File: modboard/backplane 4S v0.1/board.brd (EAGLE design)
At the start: 50 x 42 mm, 20 parts

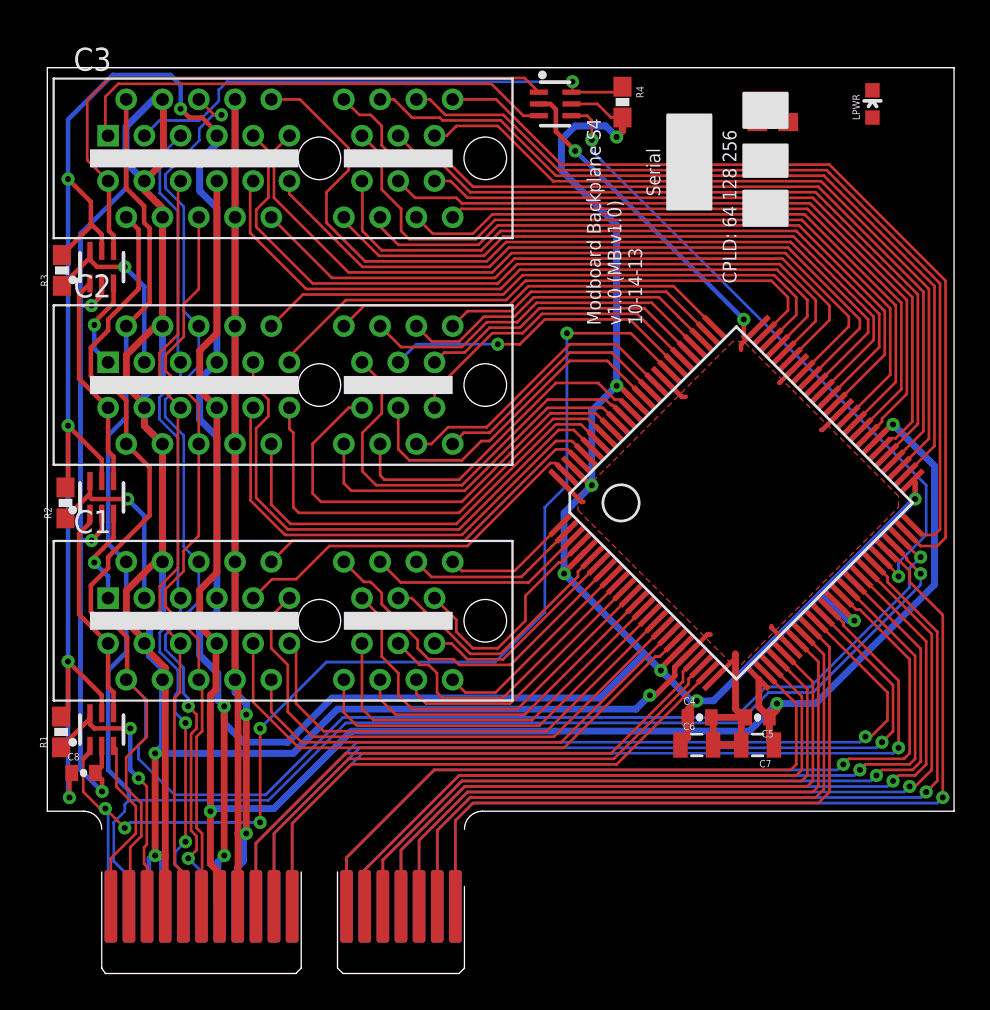
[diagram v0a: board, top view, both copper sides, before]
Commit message: rerouted parts of the modboard backplane to put the {2,3}{D,E} lanes on the NC lines
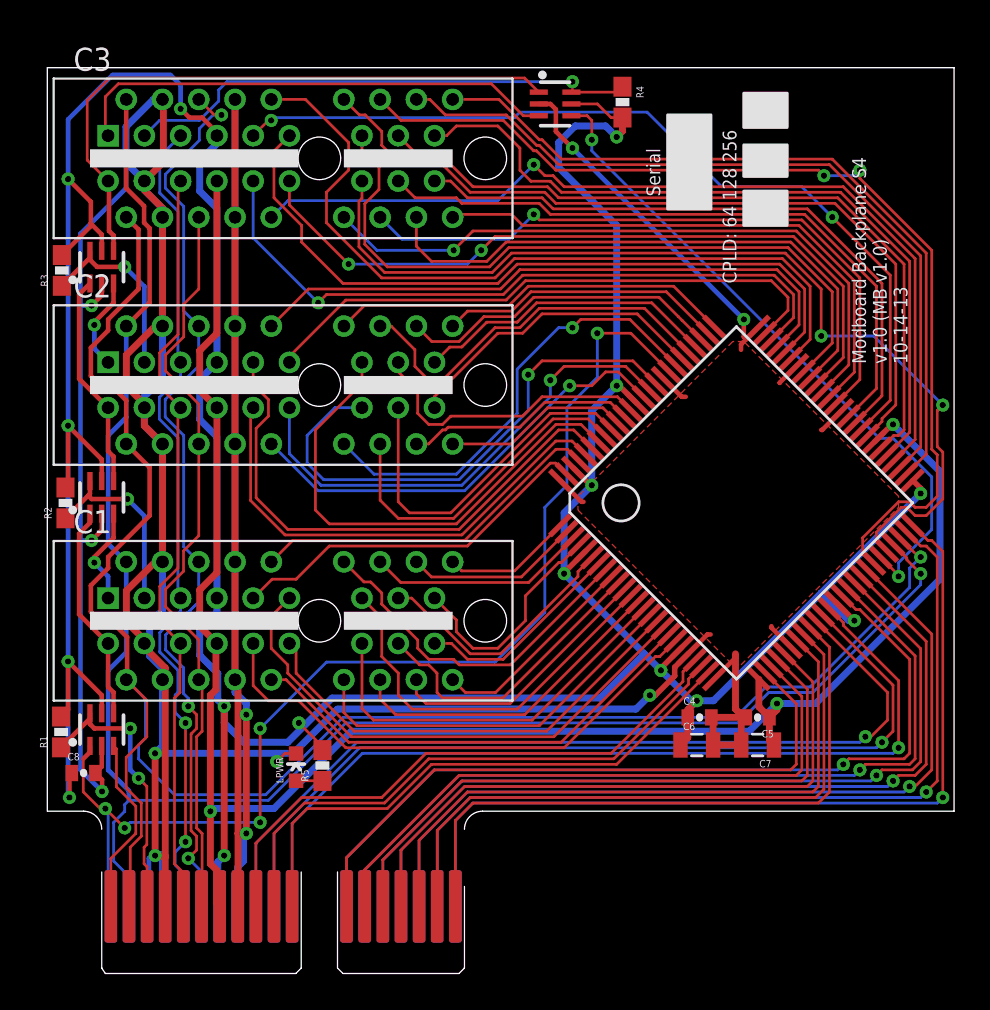
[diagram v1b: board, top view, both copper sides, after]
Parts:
- moved LPWR 48.5 mm to (13.7, 11.4)
- moved R5 43.3 mm to (15.2, 11.5), turned to 90 degrees
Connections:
- net 0A2: now also U$1.49; no longer U$1.44
- net 0A3: now also U$1.50; no longer U$1.46
- net 2A0: now also U$1.89; no longer U$1.82
- net 2A2: now also U$1.79; no longer U$1.80
- net 2B0: now also U$1.92; no longer U$1.87
- net 2B1: now also U$1.90; no longer U$1.85
- net 2B3: now also U$1.91; no longer U$1.86
- net 2C0: now also U$1.72; no longer U$1.73
- net 2C3: now also U$1.94; no longer U$1.90
- net 2D0: now also U$1.87; no longer U$1.94
- net 2D1: now also U$1.86; no longer U$1.93
- net 2D2: now also U$1.82; no longer U$1.91
- net 2D3: now also U$1.85; no longer U$1.92
- net 2E0: now also U$1.80; no longer U$1.79
- net 2E1: now also U$1.93; no longer U$1.89
- net 3A0: now also U$1.56; no longer U$1.54
- net 3A1: now also U$1.53; no longer U$1.50
- net 3A2: now also U$1.55; no longer U$1.53
- net 3A3: now also U$1.52; no longer U$1.49
- net 3B0: now also U$1.61; no longer U$1.58
- net 3B1: now also U$1.67; no longer U$1.60
- net 3B2: now also U$1.60; no longer U$1.56
- net 3B3: now also U$1.64; no longer U$1.59
- net 3C0: now also U$1.70; no longer U$1.66
- net 3C1: now also U$1.71; no longer U$1.68
- net 3C2: now also U$1.58; no longer U$1.55
- net 3C3: now also U$1.68; no longer U$1.61
- net 3D0: now also U$1.54; no longer U$1.70
- net 3D1: now also U$1.66; no longer U$1.67
- net 3D3: now also U$1.46; no longer U$1.64
- net 3E0: now also U$1.44; no longer U$1.52
- net 3E2: now also U$1.59; no longer U$1.71
- net 3E3: now also U$1.73; no longer U$1.72
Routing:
- net 3D3: track 39.8 -> 53.4 mm, vias 0 -> 2
- net 3D0: track 37.5 -> 50.5 mm, vias 0 -> 1
- net 3E0: track 45.8 -> 55.1 mm, vias 0 -> 2
- net 3A3: track 48.2 -> 42.3 mm
- net 3E2: track 42.7 -> 48.5 mm, vias 0 -> 2
- net 2D2: track 19.7 -> 25.0 mm, vias 0 -> 1
- net 3A1: track 48.5 -> 43.5 mm
- net 3B1: track 36.7 -> 32.2 mm
- net 3B3: track 35.0 -> 30.7 mm
- net 3C0: track 47.7 -> 43.6 mm
- net 2D3: track 25.3 -> 29.2 mm, vias 0 -> 1
- net 2C3: track 24.0 -> 27.8 mm
- net 2B1: track 16.4 -> 12.7 mm
- net 2B3: track 13.8 -> 10.3 mm
- net 3C3: track 42.7 -> 39.5 mm
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
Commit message: finished the base modboards
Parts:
- added C10, C11, C9: 100nF, kmod-passives:0402-CAP
- C0: value PCIE-X1EDGE -> MB-V1-X1
- moved C5 0.20 mm to (39.2, 14.0)
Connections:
- removed net 0E3: C0.B9, U$1.22
- removed net 1E3: C1.B9, U$1.19
- net 0D2: now also U$1.28; no longer U$1.27
- net 0D3: now also U$1.29; no longer U$1.28
- net 0E0: now also C0.A9, U$1.35; no longer C0.A14, U$1.41
- net 0E1: now also C0.B9, U$1.22; no longer C0.B14, U$1.29
- net 0E2: now also C0.A14, U$1.41; no longer C0.A9, U$1.35
- net 1.8V: now also C11.1
- net 1A0: now also U$1.7; no longer U$1.6
- net 1A1: now also U$1.3; no longer U$1.2
- net 1A2: now also U$1.6; no longer U$1.4
- net 1A3: now also U$1.2; no longer U$1.1
- net 1B0: now also U$1.11; no longer U$1.10
- net 1B1: now also U$1.12; no longer U$1.11
- net 1B2: now also U$1.8; no longer U$1.7
- net 1B3: now also U$1.10; no longer U$1.9
- net 1C2: now also U$1.9; no longer U$1.8
- net 1C3: now also U$1.13; no longer U$1.12
- net 1E0: now also C1.A9, U$1.1; no longer C1.A14, U$1.3
- net 1E1: now also C1.B9, U$1.19; no longer C1.B14, U$1.13
- net 1E2: now also C1.A14, U$1.4; no longer C1.A9, U$1.99
- net 2E0: now also C2.A9, U$1.95; no longer C2.A14, U$1.80
- net 2E1: now also C2.B9, U$1.96; no longer C2.B14, U$1.93
- net 2E2: now also C2.A14, U$1.80; no longer C2.A9, U$1.95
- net 2E3: now also C2.B14, U$1.93; no longer C2.B9, U$1.96
- net 3.3V: now also C10.1, C9.1
- net 3E0: now also C3.A9, U$1.59; no longer C3.A14, U$1.44
- net 3E1: now also C3.B9, U$1.73; no longer C3.B14, U$1.63
- net 3E2: now also C3.A14, U$1.44; no longer C3.A9, U$1.59
- net 3E3: now also C3.B14, U$1.63; no longer C3.B9, U$1.73
- net G0: now also U$1.27
- net GND: now also C0.B14, C1.B14, C10.2, C11.2, C9.2
- net GRST: now also U$1.99
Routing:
- net GND: track 219.7 -> 265.2 mm, vias 9 -> 11
- net G0: track 41.4 -> 80.7 mm, vias 0 -> 5
- net 0E3: track 32.2 -> 0.00 mm
- net 1E3: track 29.5 -> 0.00 mm
- net GRST: track 42.3 -> 70.5 mm
- net 1.8V: track 103.4 -> 114.9 mm, vias 3 -> 6
- net 1E1: track 18.2 -> 29.2 mm
- net 2E2: track 30.0 -> 21.4 mm
- net 2E3: track 26.9 -> 18.3 mm
- net 2E0: track 21.4 -> 29.8 mm
- net 1E2: track 20.6 -> 12.3 mm
- net 2E1: track 18.6 -> 26.7 mm
- net 3.3V: track 221.6 -> 228.3 mm, vias 16 -> 18
- net 3E2: track 48.5 -> 55.1 mm
- net 3E0: track 55.1 -> 48.5 mm
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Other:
- board text added: "MB Backplane S4 v1.0 MB v1.0 10-21-13"
- board text removed: "Modboard Backplane S4 v1.0 (MB v1.0) 10-14-13"
